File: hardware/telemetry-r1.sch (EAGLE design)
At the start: 24 parts, among them IC1 COPERNICUSSMD, IC2 TPS79033, U1 STM32L07C, Y1 32768, Y2 8M

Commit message: Update schematic. Still no layout, but the majority of components are on the sheet, including temp/humidity sensors, HX1, regulators, and SD card.
Many connectors are still missing. No LoRA footprint has yet been added.
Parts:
- removed U1: STM32L07C, stm32xx:STM32L07C
- added C16, C17, C23, C26, C27, C28, C29: 0.1u, SparkFun-Passives:CAP0805
- added C18, C22: 1u, SparkFun-Passives:CAP0805
- added C19, C20: 10u, SparkFun-Passives:CAP0805
- added C21: 100u, SparkFun-Passives:CAP_POLPTH2
- added C24: 1.0u, SparkFun-Passives:CAP0805
- added C25: 100p, SparkFun-Passives:CAP0805
- added D1: 12V, SparkFun-DiscreteSemi:DIODE-ZENER5.6V
- added D2: 5.6V, SparkFun-DiscreteSemi:DIODE-ZENER5.6V
- added D3: COM-10866, SparkFun-LED:LED-TRICOLOR-5050NO_IC
- added FRAME2: FRAME-LETTERNO_PACKAGE, SparkFun-Aesthetics:FRAME-LETTERNO_PACKAGE
- added IC3: 74HC137, 74xx-us:74LS137D
- added IC4: STM32L073CZT6, stm32xx:STM32L07C
- added IC5: TPS62160, HAB:TPS62160
- added IC6: HX1, HAB:HX1
- added IC7: LMP7702, SparkFun-AnalogIC:OPAMP-DUALU
- added IC8: ADXL345, SparkFun-Sensors:ADXL345
- added IC9: HIH9131, SparkFun-AnalogIC:HIH6131
- added J1: I2C1, SparkFun-Connectors:I2C_STANDARD_NO_SILK
- added J2: I2C2, SparkFun-Connectors:I2C_STANDARD_NO_SILK
- added J3: BOTTOM, SparkFun-Connectors:M102MM
- added J4: USD-SOCKET, SparkFun-Connectors:USD-SOCKET
- added JP1: BAT, SparkFun-Connectors:M02PTH
- added L2: FERRITE, HAB:INDUCTOR1206
- added R10: 4.7K, SparkFun-Passives:RESISTOR0805-RES
- added R10\: 430K, SparkFun-Passives:RESISTOR0805-RES
- added R11: 82K, SparkFun-Passives:RESISTOR0805-RES
- added R12, R4, R7, R9: 10K, SparkFun-Passives:RESISTOR0805-RES
- added R13, R14: 220, SparkFun-Passives:RESISTOR0805-RES
- added R15: 330, SparkFun-Passives:RESISTOR0805-RES
- added R16: 1.5M, SparkFun-Passives:RESISTOR0805-RES
- added R17: 470K, SparkFun-Passives:RESISTOR0805-RES
- added R18, R5, R8: 100, SparkFun-Passives:RESISTOR0805-RES
- added R2, R6: 10K, SparkFun-Passives:RESISTOR-ARRAY0603-ARV
- added R3: 100, SparkFun-Passives:RESISTOR-ARRAY0603-ARV
- added S2: BTN, HAB:SWITCH
- IC2: value TPS79033 -> TPS70933
- L1: value FERRITE -> 2.2u; device SparkFun-Passives:RESISTOR0805-RES -> HAB:INDUCTOR1008
- S1: value RESET -> RST; device SparkFun-Electromechanical:SWITCH-MOMENTARY-2PTH -> HAB:SWITCH
- Y1: device SparkFun-FreqCtrl:CRYSTALTC26H -> HAB:CRYSTAL
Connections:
- new net +9V: C18.1, C21.+, D1.C, IC5.EN, IC5.VIN, JP1.2
- new net A+: C25.2, IC7A.-IN, IC7B.+IN, R16.1, R17.2
- new net A-: IC7B.-IN, R18.1
- new net A2O: IC7A.+IN, IC7A.OUT
- new net ADXL_SDO: IC8.SDO, R12.2
- new net AGND: IC1.GND@2, IC1.GND@3, IC6.RFGND
- new net BC: D3.BLU-C, R13.2
- new net BTN: IC4.PC13, R7.1, S2.2
- new net B_CSADC: J3.9, R3A.1
- new net B_CSHUM: J3.5, R3D.1
- new net B_CSPRS: J3.7, R3B.1
- new net B_MISO: J3.6, R3C.1
- new net B_MOSI: J3.4, R5.2
- new net B_SCK: J3.2, R8.2
- new net CSA0: IC3A.A, IC4.PB6, R6B.2
- new net CSA1: IC3A.B, IC4.PB7, R6C.2
- new net CSA2: IC3A.C, IC4.PB12
- new net CSADC: IC3A.Y3, R3A.2
- new net CSBHUM: IC3A.Y4, R3D.2
- new net CSHUM: IC3A.Y2, IC9.SCL
- new net CSLAT: IC3A.GL, IC4.PA15, R6A.2
- new net CSLORA: IC3A.Y1
- new net CSPRS: IC3A.Y5, R3B.2
- new net CSSD: IC3A.Y0, J4.CS
- new net D+: IC4.PA12
- new net D-: IC4.PA11
- new net DAC: C25.1, IC4.PA4
- new net FB5: IC5.FB, R10\.1, R11.2
- new net GC: D3.GRN-C, R14.2
- new net GPSBOOT: IC1.BOOT, R4.1
- new net GPSRX: IC1.TXD-B, IC4.PB11, R2D.2
- new net GPSTX: IC1.RXD-B, IC4.PB10
- new net HXEN: IC4.PA3, IC6.EN, R10.1
- new net INT: IC8.INT1
- new net INT2: IC8.INT2
- new net LEDB: IC4.PB1, R13.1
- new net LEDG: IC4.PB0, R14.1
- new net LEDR: IC4.PA7, R15.1
- new net MISO: IC4.PB4, IC9.AL_H, J4.DO, R3C.2
- new net MOSI: IC4.PB5, J4.DI, R5.1
- new net N$1: C28.1, IC9.VCORE
- new net PG5: IC5.PG, R9.1
- new net PPS: IC1.PPS
- new net RC: D3.RED-C, R15.2
- new net RXA: IC1.RXD-A, R2B.2
- new net SCK: IC4.PB3, IC9.SDA, J4.SCK, R8.1
- new net SCL: IC4.PB8, IC8.SCL, J1.4, J2.4
- new net SDA: IC4.PB9, IC8.SDA, J1.3, J2.3
- new net SW5: IC5.OUT, L1.1
- new net TEMPB: IC4.PA6
- new net TEMPG: IC4.PA2
- new net TEMPH: IC4.PA1
- new net TXA: IC1.TXD-A, R2C.2
- new net TXD: IC6.TXD, IC7B.OUT, R18.2
- new net VDIV: IC4.PA5
- new net XSTBY: IC1.XSTANDBY, IC4.PB2, R2A.2
- net !RST!: now also IC1.XRESET, IC4.!RST!; no longer U1.!RST!
- net 3.3V: now also C16.1, C23.1, C24.1, C27.1, C29.1, IC3A.G1, IC3P.VCC, IC4.VDD, IC4.VDD_USB, IC4.VLCD, IC8.CS, IC8.VDD, IC8.VS, IC9.VDD, J1.2, J2.2, J3.10, J3.8, J4.VCC, L2.1, R2A.1, R2B.1, R2C.1, R2D.1, R4.2, R6A.1, R6B.1, R6C.1, R6D.1, R7.2; no longer L1.1, U1.VDD, U1.VDD_USB, U1.VLCD
- net 5V: now also C17.1, C19.1, C20.1, C22.1, C26.1, D2.C, D3.BLU-A, D3.GRN-A, D3.RED-A, IC5.VOS, IC6.VCC, IC7A.V+, L1.2, R10.2, R10\.2, R16.2, R9.2
- net BOOT0: now also IC4.BOOT0, R6D.2; no longer U1.BOOT0
- net GND: now also C16.2, C17.2, C18.2, C19.2, C20.2, C21.-, C22.2, C23.2, C24.2, C26.2, C27.2, C28.2, C29.2, D1.A, D2.A, IC3A.G2, IC3P.GND, IC4.VSS, IC4.VSSA, IC5.GND, IC6.GND, IC7A.V-, IC8.GND@2, IC8.GND@4, IC8.GND@5, IC9.GND, J1.1, J2.1, J3.1, J3.3, J4.CD1, J4.CD2, J4.GND, J4.SHIELD@1, J4.SHIELD@3, JP1.1, R11.1, R12.1, R17.1, S2.1; no longer IC1.GND@2, IC1.GND@3, U1.VSS, U1.VSSA
- net MCO: now also IC4.PA8; no longer U1.PA8
- net OSC32_IN: now also IC4.OSC32_IN; no longer U1.OSC32_IN
- net OSC32_OUT: now also IC4.OSC32_OUT; no longer U1.OSC32_OUT
- net OSC_IN: now also IC4.OSC_IN; no longer U1.OSC_IN
- net OSC_OUT: now also IC4.OSC_OUT; no longer U1.OSC_OUT
- net SWCLK: now also IC4.PA14; no longer U1.PA14
- net SWDIO: now also IC4.PA13; no longer U1.PA13
- net VDDA: now also IC4.VDDA, L2.2; no longer L1.2, U1.VDDA
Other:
- note added: "535-10241-1-ND"
- note added: "887-1233-ND"
- note added: "HOUSING: 455-1151-ND CRIMP: 455-1127-1-ND PLUG: 455-1712-ND"
- note added: "L1: CVH252009-2R2MCT-ND C19-C20: 490-5523-1-ND C21: 493-10772-1-ND D1: ESD12VD3-TPMSCT-ND"
- note added: "NC"
- note added: "Optional Adafruit 619 fits 1516-1131-1-ND fits"
- note added: "PWM IN/OUT"
- note added: "YC164J-100CT-ND"
- note added: "YC164J-10KCT-ND"
- moved on the sheet: C1, C10, C11, C12, C13, C14, C15, C2, C3, C4, C5, C6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

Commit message: Add more connectors and parts to schematic. Please review it and let me know what is still missing. In particular, no LoRA module is on board.
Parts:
- added C30, C31, C32: 0.1u, SparkFun-Passives:CAP0805
- added D4, D5, D6: CM1213A, HAB:CM1213A
- added J10: TEMP_BAT, SparkFun-Connectors:M03JST-PTH
- added J11: DNP, SparkFun-Connectors:M06LOCK
- added J5: BAT, SparkFun-Connectors:M02PTH
- added J6, J7: SMA_EDGE, SparkFun-Connectors:SMA_EDGE
- added J8: TEMP_GPS, SparkFun-Connectors:M03JST-PTH
- added J9: TEMP_HOT, SparkFun-Connectors:M03JST-PTH
- added JP2: GND, SparkFun-Passives:JUMPER-PAD-2-NC_BY_TRACE
- added R19: 470K, SparkFun-Passives:RESISTOR0805-RES
- added R20: 180K, SparkFun-Passives:RESISTOR0805-RES
- added R21: DNP, SparkFun-Passives:RESISTOR0805-RES
- JP1: value BAT -> GND; device SparkFun-Connectors:M02PTH -> SparkFun-Passives:JUMPER-PAD-2-NC_BY_TRACE
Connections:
- net N$1 renamed VCORE
- new net AL_L: IC9.AL_L
- new net RF_GPS: IC1.RFIN, J7.SIGNAL
- new net RF_HX1: IC6.RFOUT, J6.SIGNAL
- new net RGND: IC6.RFGND, J6.GND@0, J6.GND@1, J6.GND@2, J6.GND@3, JP2.1
- net !RST!: now also J11.5
- net +9V: now also J5.2, R19.2; no longer JP1.2
- net 3.3V: now also C30.1, C31.1, C32.1, D4.VCC, D5.VCC, D6.VCC, J10.2, J11.1, J8.2, J9.2
- net AGND: now also J7.GND@0, J7.GND@1, J7.GND@2, J7.GND@3, JP1.1; no longer IC6.RFGND
- net B_CSADC: now also D4.CH3
- net B_CSHUM: now also D4.CH2
- net B_CSPRS: now also D4.CH4
- net B_MISO: now also D4.CH1
- net B_MOSI: now also D5.CH4
- net B_SCK: now also D5.CH1
- net DAC: now also R21.2
- net GND: now also C30.2, C31.2, C32.2, D4.GND, D5.GND, D6.GND, J10.1, J11.3, J5.1, J8.1, J9.1, JP1.2, JP2.2, R20.1, R21.1; no longer JP1.1
- net SCL: now also D5.CH3
- net SDA: now also D5.CH2
- net SWCLK: now also J11.2
- net SWDIO: now also J11.4
- net TEMPB: now also D6.CH4, J10.3
- net TEMPG: now also D6.CH3, J8.3
- net TEMPH: now also D6.CH1, J9.3
- net VDIV: now also R19.1, R20.2
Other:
- note added: "HOUSING: 455-1151-ND CRIMP: 455-1127-1-ND VERT: 455-1712-ND SIDE: 455-1727-ND"
- note added: "Single Point Ground"
- note removed: "HOUSING: 455-1151-ND CRIMP: 455-1127-1-ND PLUG: 455-1712-ND"
- moved on the sheet: C11, C12, C17, C22, C23, C24, C28, C29, D3, IC1, IC3, IC6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

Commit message: Start layout for telemetry board. Initially had it almost 80% done, but started over to get a better route on those last few nets
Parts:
- added C33, C34: 0.1u, SparkFun-Passives:CAP0805
- added C35, C36: 1u, SparkFun-Passives:CAP0805
- added IC10: TPS70933, texas:TPS77033
- added J12: INSOL, SparkFun-Connectors:M03JST-PTH
- added J13: LORA, HAB:1X08
- added R22: 100, SparkFun-Passives:RESISTOR0805-RES
- added R23: 4.7K, SparkFun-Passives:RESISTOR0805-RES
- added R24, R25: 10K, SparkFun-Passives:RESISTOR0805-RES
- IC3: device 74xx-us:74LS137D -> HAB:74LS137PW
- R10: value 4.7K -> 10K
- R6: device SparkFun-Passives:RESISTOR-ARRAY0603-ARV -> SparkFun-Passives:RESISTOR0805-RES
- Y2: device SparkFun-FreqCtrl:CRYSTALHC49UV -> SparkFun-FreqCtrl:CRYSTALSMD
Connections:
- new net B_LORA: J13.5, R22.2
- new net INSOL: D6.CH2, IC4.PA6, J12.3
- new net USIN: IC4.PB14
- new net USOUT: IC4.PB15
- new net USRES: IC4.PB13
- new net VS: C23.1, C24.1, C29.1, C30.1, C31.1, C32.1, C33.1, C35.1, C36.1, D6.VCC, IC10.OUT, IC8.CS, IC8.VDD, IC8.VS, IC9.VDD, J10.1, J12.1, J3.10, J3.8, J8.1, J9.1
- new net XRESET: IC1.XRESET, R24.2
- net !RST!: now also J13.7; no longer IC1.XRESET
- net 3.3V: now also J13.8, R10.2, R24.1, R25.1, R6.2; no longer C23.1, C24.1, C29.1, C30.1, C31.1, C32.1, D6.VCC, IC8.CS, IC8.VDD, IC8.VS, IC9.VDD, J10.2, J3.10, J3.8, J8.2, J9.2, R2A.1, R6A.1, R6B.1, R6C.1, R6D.1
- net 5V: now also C34.1, IC10.IN, R23.2; no longer R10.2
- net BOOT0: now also R10.1; no longer R6D.2
- net B_MISO: now also J13.6
- net B_MOSI: now also D5.CH1, J13.4; no longer D5.CH4
- net B_SCK: now also D5.CH4, J13.2; no longer D5.CH1
- net CSA0: now also IC4.PB7; no longer IC4.PB6, R6B.2
- net CSA1: now also IC4.PB6; no longer IC4.PB7, R6C.2
- net CSADC: now also IC3A.Y5; no longer IC3A.Y3
- net CSBHUM: now also IC3A.Y3; no longer IC3A.Y4
- net CSLAT: now also R6.1; no longer R6A.2
- net CSLORA: now also R22.1
- net CSPRS: now also IC3A.Y4; no longer IC3A.Y5
- net GND: now also C33.2, C34.2, C35.2, C36.2, IC10.GND, J10.2, J12.2, J13.1, J13.3, J8.2, J9.2; no longer J10.1, J8.1, J9.1
- net HXEN: now also IC4.PA5, R23.1; no longer IC4.PA3, R10.1
- net LEDG: now also IC4.PA7; no longer IC4.PB0
- net LEDR: now also IC4.PB0; no longer IC4.PA7
- net SCL: now also D5.CH2; no longer D5.CH3
- net SDA: now also D5.CH3; no longer D5.CH2
- net TEMPB: now also IC4.PA1; no longer IC4.PA6
- net TEMPG: now also IC4.PA0; no longer IC4.PA2
- net TEMPH: now also IC4.PA2; no longer IC4.PA1
- net VDIV: now also IC4.PA3; no longer IC4.PA5
- net XSTBY: now also R25.2; no longer R2A.2
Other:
- note added: "HOUSING: 455-1151-ND CRIMP: 455-1127-1-ND SIDE: 455-1727-ND"
- note added: "L1: CVH252009-2R2MCT-ND C19-C20: 490-5523-1-ND C21: 493-10772-1-ND D1: ESD12VD3-TPMSCT-ND D2: DESD5V0U1BA-7DICT-ND"
- note added: "PLUG: 455-1710-ND"
- note removed: "HOUSING: 455-1151-ND CRIMP: 455-1127-1-ND VERT: 455-1712-ND SIDE: 455-1727-ND"
- note removed: "L1: CVH252009-2R2MCT-ND C19-C20: 490-5523-1-ND C21: 493-10772-1-ND D1: ESD12VD3-TPMSCT-ND"
- note removed: "PWM IN/OUT"
- moved on the sheet: R10

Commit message: Fully route telemtery PCB, please review
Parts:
- added D10, D7, D8, D9: 5.6V, SparkFun-DiscreteSemi:DIODE-ZENER5.6V
- D4, D5: value CM1213A -> 5.6V; device HAB:CM1213A -> SparkFun-DiscreteSemi:DIODE-ZENER5.6V
- renumbered R10 to R26
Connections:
- net !RST!: no longer J13.7
- net 3.3V: now also D10.C, J13.7; no longer D4.VCC, D5.VCC
- net B_CSADC: now also J3.7, R3B.1; no longer D4.CH3, J3.9, R3A.1
- net B_CSHUM: now also J3.3; no longer D4.CH2, J3.5
- net B_CSPRS: now also J3.6, R3C.1; no longer D4.CH4, J3.7, R3B.1
- net B_LORA: now also J13.3; no longer J13.5
- net B_MISO: now also D4.C, J3.9, R3A.1; no longer D4.CH1, J3.6, R3C.1
- net B_MOSI: now also D9.C, J13.2, J3.2, R8.2; no longer D5.CH1, J13.4, J3.4, R5.2
- net B_SCK: now also D8.C, J13.4, J3.4, R5.2; no longer D5.CH4, J13.2, J3.2, R8.2
- net CSADC: now also R3B.2; no longer R3A.2
- net CSPRS: now also R3C.2; no longer R3B.2
- net GND: now also D10.A, D4.A, D5.A, D7.A, D8.A, D9.A, J13.5, J3.5; no longer D4.GND, D5.GND, J13.3, J3.3
- net MISO: now also R3A.2; no longer R3C.2
- net MOSI: now also R8.1; no longer R5.1
- net SCK: now also R5.1; no longer R8.1
- net SCL: now also D7.C; no longer D5.CH2
- net SDA: now also D5.C; no longer D5.CH3
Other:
- note added: "L1: CVH252009-2R2MCT-ND C19-C20: 490-5523-1-ND C21: 493-10772-1-ND D1: ESD12VD3-TPMSCT-ND D2, D5, D7-D9: DESD5V0U1BA-7DICT-ND"
- note removed: "L1: CVH252009-2R2MCT-ND C19-C20: 490-5523-1-ND C21: 493-10772-1-ND D1: ESD12VD3-TPMSCT-ND D2: DESD5V0U1BA-7DICT-ND"
- moved on the sheet: R22, R3D, R5

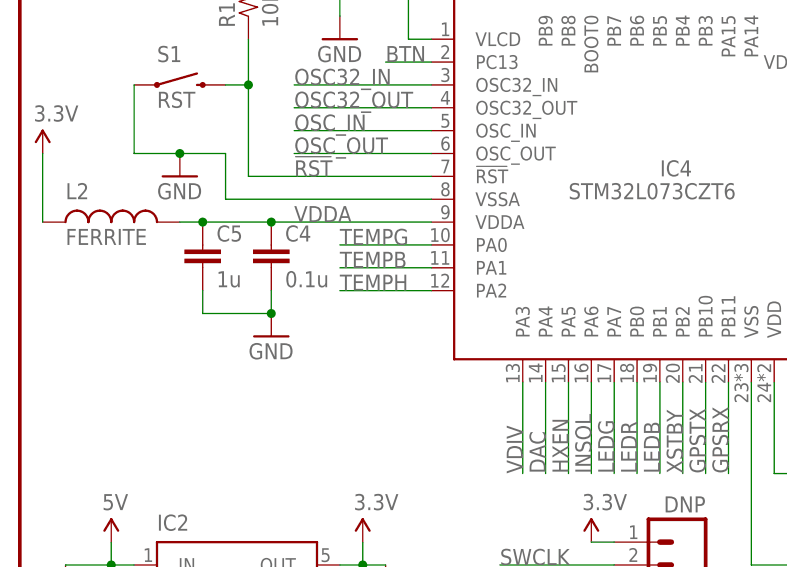
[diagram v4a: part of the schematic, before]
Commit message: Fix a few issues on the telemetry PCB. Add schematic (no layout) for bottom/sensors board.
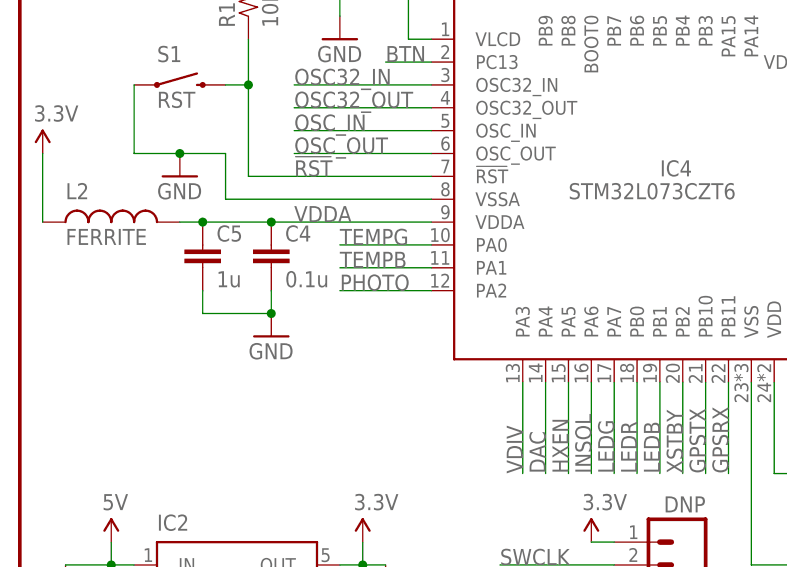
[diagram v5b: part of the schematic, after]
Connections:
- new net PHOTO: IC4.PA2
- net TEMPH: no longer IC4.PA2
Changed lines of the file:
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@@
 <?xml version="1.0" encoding="utf-8"?>
 <!DOCTYPE eagle SYSTEM "eagle.dtd">
-<eagle version="7.4.0">
+<eagle version="7.6.0">
 <drawing>
 <settings>
@@
 <label x="345.44" y="7.62" size="1.778" layer="95" rot="R90"/>
 </segment>
-<segment>
-<pinref part="IC4" gate="G$1" pin="PA2"/>
-<wire x1="35.56" y1="50.8" x2="45.72" y2="50.8" width="0.1524" layer="91"/>
-<label x="35.56" y="50.8" size="1.778" layer="95"/>
-</segment>
 </net>
 <net name="HXEN" class="0">
@@
 </segment>
 </net>
+<net name="PHOTO" class="0">
+<segment>
+<pinref part="IC4" gate="G$1" pin="PA2"/>
+<wire x1="35.56" y1="50.8" x2="45.72" y2="50.8" width="0.1524" layer="91"/>
+<label x="35.56" y="50.8" size="1.778" layer="95"/>
+</segment>
+</net>
